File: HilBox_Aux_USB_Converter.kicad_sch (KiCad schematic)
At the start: 25 parts, among them J5 USB_C_Plug_USB2.0, U10 FT232RL, U4 USB6B1RL

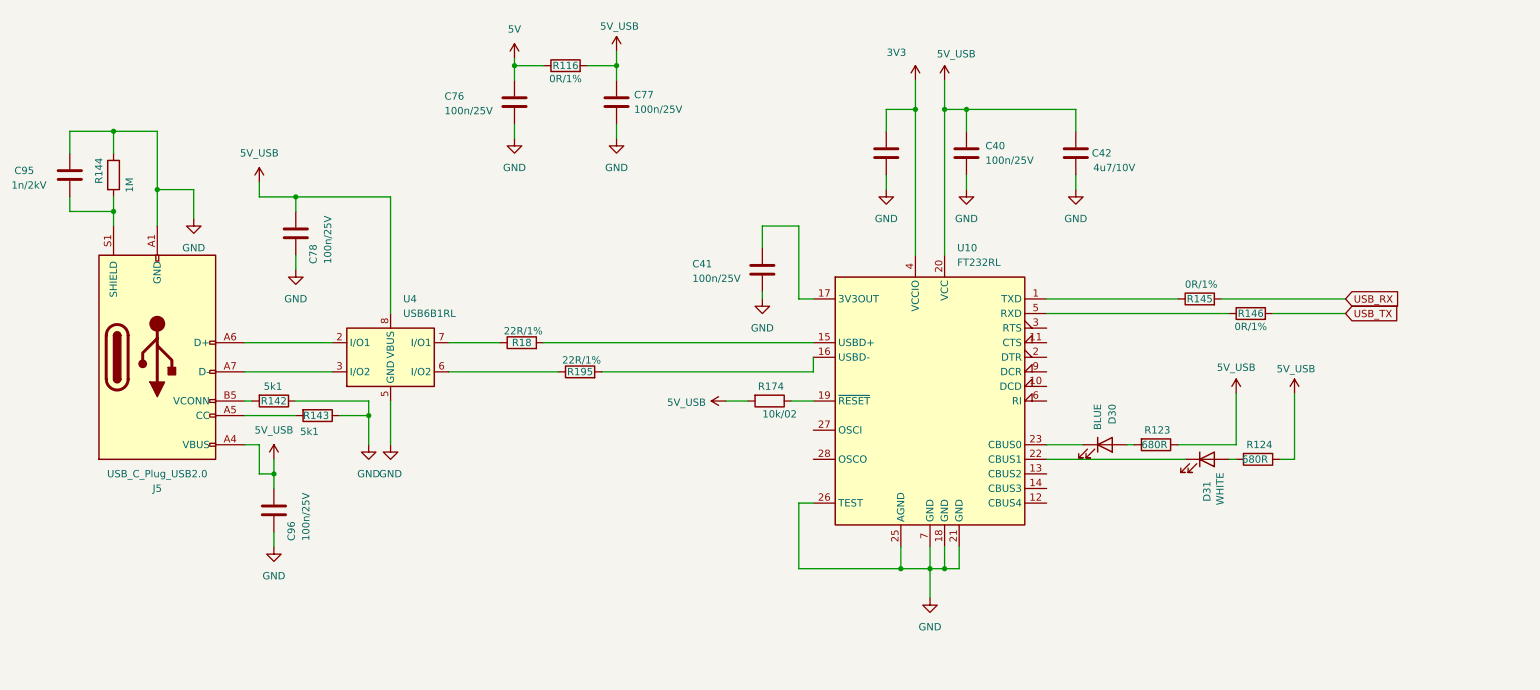
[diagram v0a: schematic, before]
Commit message: Modification in half of target
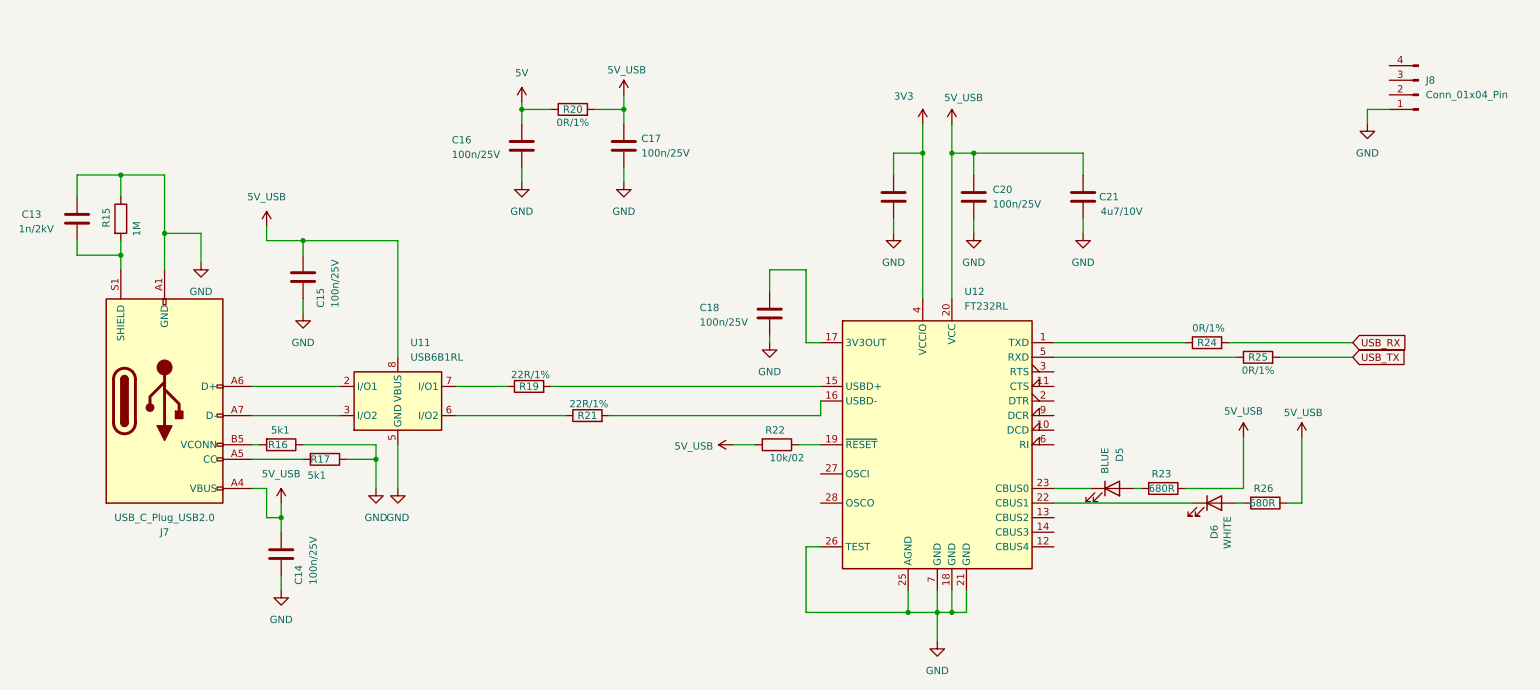
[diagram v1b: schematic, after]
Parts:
- removed C39, C40, C41, C76, C77, C78, C96: 100n/25V, Capacitor_SMD:C_0402_1005Metric, symbol Device:C
- removed C42: 4u7/10V, Capacitor_SMD:C_0402_1005Metric, symbol Device:C
- removed C95: 1n/2kV, Capacitor_SMD:C_1206_3216Metric, symbol Device:C
- removed D30: BLUE, LED_SMD:LED_0603_1608Metric, symbol Device:LED
- removed D31: WHITE, LED_SMD:LED_0603_1608Metric, symbol Device:LED
- removed J5: USB_C_Plug_USB2.0, Connector_USB:USB_C_Receptacle_GCT_USB4105-xx-A_16P_TopMnt_Horizontal, symbol Connector:USB_C_Plug_USB2.0
- removed R116, R145, R146: 0R/1%, Resistor_SMD:R_0603_1608Metric, symbol Device:R
- removed R123, R124: 680R, Resistor_SMD:R_0603_1608Metric, symbol Device:R
- removed R142, R143: 5k1, Resistor_SMD:R_0603_1608Metric, symbol Device:R
- removed R144: 1M, Resistor_SMD:R_0603_1608Metric, symbol Device:R
- removed R174: 10k/02, Resistor_SMD:R_0402_1005Metric, symbol Device:R
- removed R18, R195: 22R/1%, Resistor_SMD:R_0402_1005Metric, symbol Device:R
- removed U10: FT232RL, Package_SO:SSOP-28_5.3x10.2mm_P0.65mm, symbol Interface_USB:FT232RL
- removed U4: USB6B1RL, Package_SO:SOIC-8_3.9x4.9mm_P1.27mm, symbol Power_Protection:USB6B1
- added C13: 1n/2kV, Capacitor_SMD:C_1206_3216Metric, symbol Device:C
- added C14, C15, C16, C17, C18, C19, C20: 100n/25V, Capacitor_SMD:C_0402_1005Metric, symbol Device:C
- added C21: 4u7/10V, Capacitor_SMD:C_0402_1005Metric, symbol Device:C
- added D5: BLUE, LED_SMD:LED_0603_1608Metric, symbol Device:LED
- added D6: WHITE, LED_SMD:LED_0603_1608Metric, symbol Device:LED
- added J7: USB_C_Plug_USB2.0, Connector_USB:USB_C_Receptacle_GCT_USB4105-xx-A_16P_TopMnt_Horizontal, symbol Connector:USB_C_Plug_USB2.0
- added J8: Conn_01x04_Pin, Connector_PinHeader_2.54mm:PinHeader_1x04_P2.54mm_Vertical, symbol Connector:Conn_01x04_Pin
- added R15: 1M, Resistor_SMD:R_0603_1608Metric, symbol Device:R
- added R16, R17: 5k1, Resistor_SMD:R_0603_1608Metric, symbol Device:R
- added R19, R21: 22R/1%, Resistor_SMD:R_0402_1005Metric, symbol Device:R
- added R20, R24, R25: 0R/1%, Resistor_SMD:R_0603_1608Metric, symbol Device:R
- added R22: 10k/02, Resistor_SMD:R_0402_1005Metric, symbol Device:R
- added R23, R26: 680R, Resistor_SMD:R_0603_1608Metric, symbol Device:R
- added U11: USB6B1RL, Package_SO:SOIC-8_3.9x4.9mm_P1.27mm, symbol Power_Protection:USB6B1
- added U12: FT232RL, Package_SO:SSOP-28_5.3x10.2mm_P0.65mm, symbol Interface_USB:FT232RL
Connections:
- net 3V3: now also C19.1, U12.4 (VCCIO)
- net 5V: now also C16.1, R20.1
- net 5V_USB: now also C14.1, C15.1, C17.1, C20.1, C21.1, J7.A4 (VBUS), J7.A9 (VBUS), J7.B4 (VBUS), J7.B9 (VBUS), R20.2, R22.2, R23.1, R26.1, U11.1 (VBUS), U11.8 (VBUS), U12.20 (VCC)
- net GND: now also C13.1, C14.2, C15.2, C16.2, C17.2, C18.2, C19.2, C20.2, C21.2, J7.A1 (GND), J7.A12 (GND), J7.B1 (GND), J7.B12 (GND), J8.1 (Pin_1), R15.1, R16.1, R17.1, U11.4 (GND), U11.5 (GND), U12.18 (GND), U12.21 (GND), U12.25 (AGND), U12.26 (TEST), U12.7 (GND)
- net USB_RX: now also R24.2
- net USB_TX: now also R25.2
- new net: C13.2, J7.S1 (SHIELD), R15.2
- new net: D5.2 (A), R23.2
- new net: J7.B5 (VCONN), R16.2
- new net: D6.2 (A), R26.2
- new net: R24.1, U12.1 (TXD)
- new net: R19.2, U12.15 (USBD+)
- new net: R21.2, U12.16 (USBD-)
- new net: C18.1, U12.17 (3V3OUT)
- new net: R22.1, U12.19 (~{RESET})
- new net: D6.1 (K), U12.22 (CBUS1)
- new net: D5.1 (K), U12.23 (CBUS0)
- new net: R25.1, U12.5 (RXD)
- new net: R21.1, U11.6 (I/O2)
- new net: J7.A6 (D+), U11.2 (I/O1)
- new net: J7.A7 (D-), U11.3 (I/O2)
- new net: R19.1, U11.7 (I/O1)
- new net: J7.A5 (CC), R17.2

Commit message: Layout 90% done
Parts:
- removed C19: 100n/25V, Capacitor_SMD:C_0402_1005Metric, symbol Device:C
- added C7: 100n/25V, Capacitor_SMD:C_0402_1005Metric, symbol Device:C
- added R14: 0R/1%, Resistor_SMD:R_0603_1608Metric, symbol Device:R
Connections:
- net 5V_USB: no longer C14.1, C15.1, C17.1, C20.1, C21.1, J7.A4 (VBUS), J7.A9 (VBUS), J7.B4 (VBUS), J7.B9 (VBUS), R20.2, R23.1, R26.1, U11.1 (VBUS), U11.8 (VBUS), U12.20 (VCC)
- net GND: now also C7.2
- net USB_RX: now also J8.3 (Pin_3)
- net USB_TX: now also J8.2 (Pin_2)
- net at C18.1, U12.17 (3V3OUT): now also R14.1
- net 5V_USB': now reaches J8.4 (Pin_4)
- net 5V_USB': now also C14.1, C15.1, C17.1, C20.1, C21.1, J7.A4 (VBUS), J7.A9 (VBUS), J7.B4 (VBUS), J7.B9 (VBUS), R20.2, R23.1, R26.1, U11.1 (VBUS), U11.8 (VBUS), U12.20 (VCC), C7.1
- net 3V3: no longer names the net of U12.4 (VCCIO)
- net 3V3: now also R14.2

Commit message: Gate finalized! PCB ordered
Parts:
- J8: JLC_PN (none) -> C7430360
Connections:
- net 5V_USB is gone; now on net 5V_USB': R22.2
- net USB_RX renamed USB_RX_OUT
- net USB_TX renamed USB_TX_OUT
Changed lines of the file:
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@@
 		)
 	)
-	(global_label "USB_RX"
+	(global_label "USB_RX_OUT"
 		(shape input)
 		(at 252.73 90.17 0)
@@
 		)
 		(property "Intersheetrefs" "${INTERSHEET_REFS}"
-			(at 262.9723 90.17 0)
+			(at 267.5685 90.17 0)
 			(effects
 				(font
@@
 		)
 	)
-	(global_label "USB_TX"
+	(global_label "USB_TX_OUT"
 		(shape input)
 		(at 252.73 92.71 0)
@@
 		)
 		(property "Intersheetrefs" "${INTERSHEET_REFS}"
-			(at 262.6699 92.71 0)
+			(at 267.2661 92.71 0)
 			(effects
 				(font
@@
 			)
 		)
+		(property "JLC_PN" "C7430360"
+			(at 264.16 46.99 0)
+			(effects
+				(font
+					(size 1.27 1.27)
+				)
+				(hide yes)
+			)
+		)
 		(pin "3"
 		)
@@
 			)
 		)
-		(property "Value" "5V_USB"
+		(property "Value" "5V_USB'"
 			(at 137.922 108.204 90)
 			(effects
